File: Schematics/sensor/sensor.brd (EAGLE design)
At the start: 27.6 x 22.9 mm, 9 parts

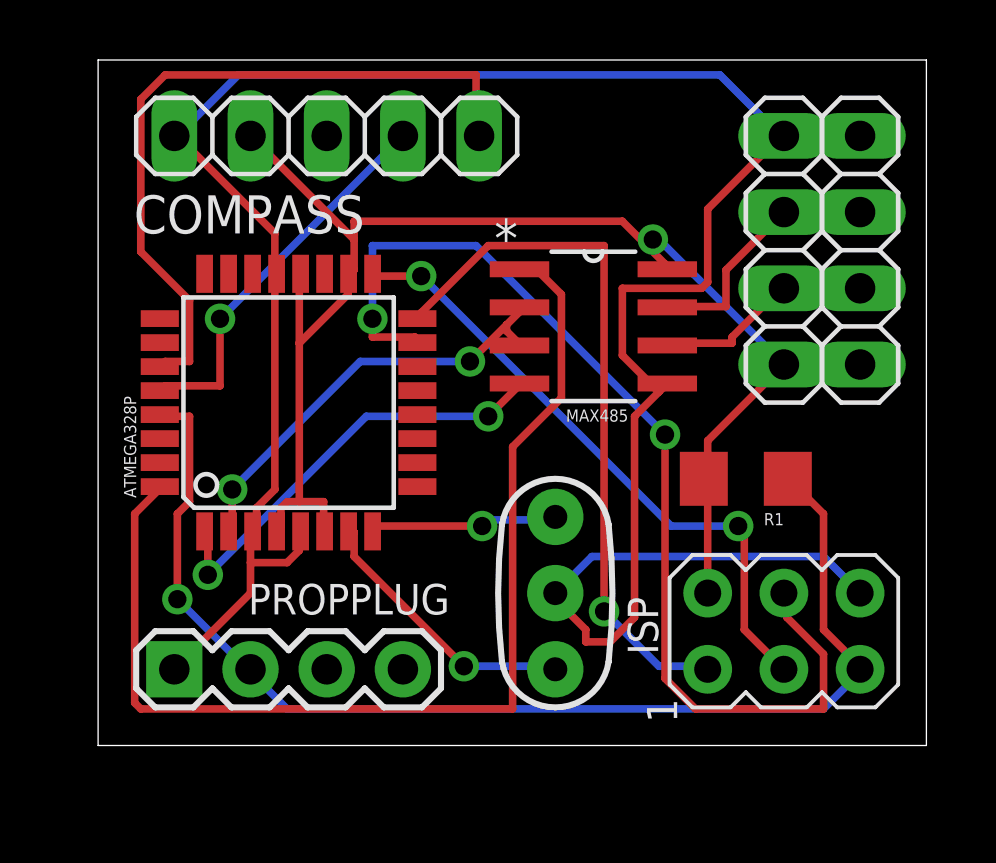
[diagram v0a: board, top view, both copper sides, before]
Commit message: Changed headers for 485 bus and added more labels.
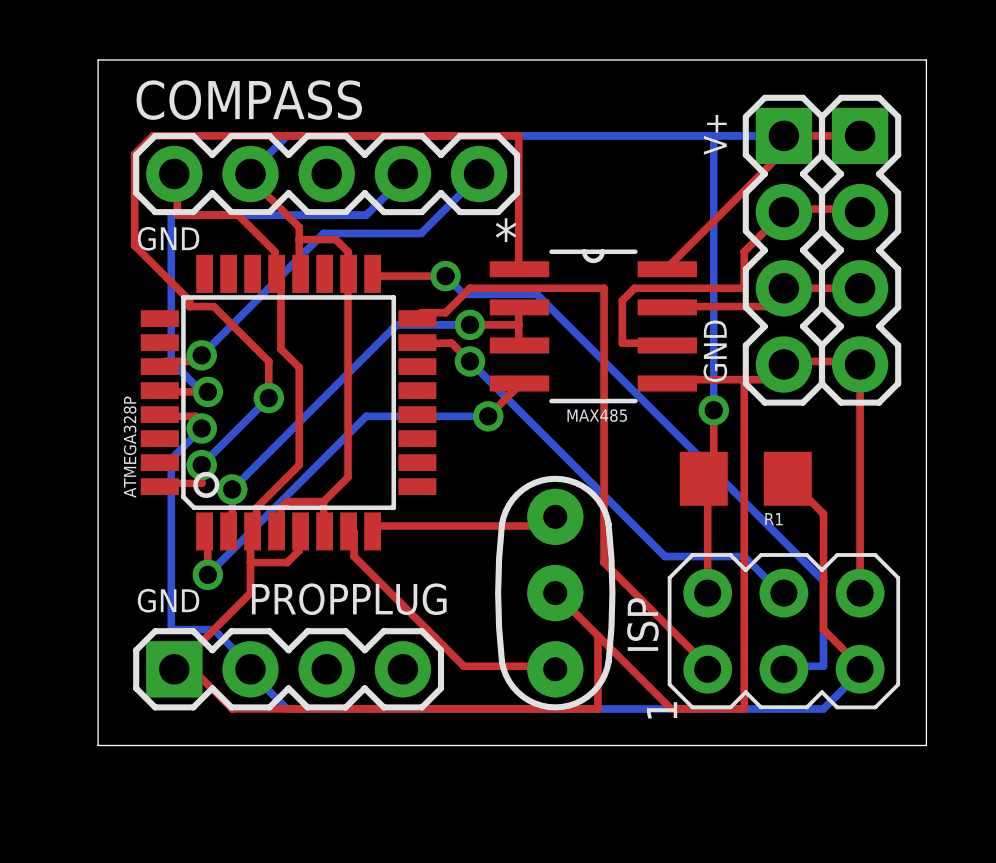
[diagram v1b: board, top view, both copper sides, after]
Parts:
- COMPASS: device pinhead:1X05 -> SparkFun-Connectors:1X05
- JP1, JP2: device pinhead:1X04 -> SparkFun-Connectors:1X04
- moved COMPASS 5.24 mm to (2.54, 19.1)
- moved JP1 4.58 mm to (22.9, 20.3), turned to 270 degrees
- moved JP2 4.58 mm to (25.4, 20.3), turned to 270 degrees
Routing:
- net N$5: track 35.3 -> 15.7 mm, vias 2 -> 1
- net SDA: track 24.1 -> 13.4 mm, vias 0 -> 1
- net 5V: track 49.7 -> 60.3 mm
- net GND: track 84.0 -> 74.3 mm
- net N$7: track 7.32 -> 13.0 mm
- net SCL: track 12.9 -> 16.5 mm
- net RO: track 36.5 -> 33.2 mm, vias 0 -> 2
- net N$4: track 23.8 -> 20.8 mm, vias 1 -> 0
- net N$3: track 21.1 -> 23.5 mm, vias 2 -> 1
- net N$8: track 8.59 -> 7.04 mm
- net RESET: track 39.6 -> 41.0 mm
- net N$2: track 6.34 -> 6.46 mm, vias 1 -> 0
- net N$1: vias 1 -> 0
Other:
- board text added: "GND"
- board text added: "V+"

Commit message: Made sensor PCB smaller. Removed through hole circuit.
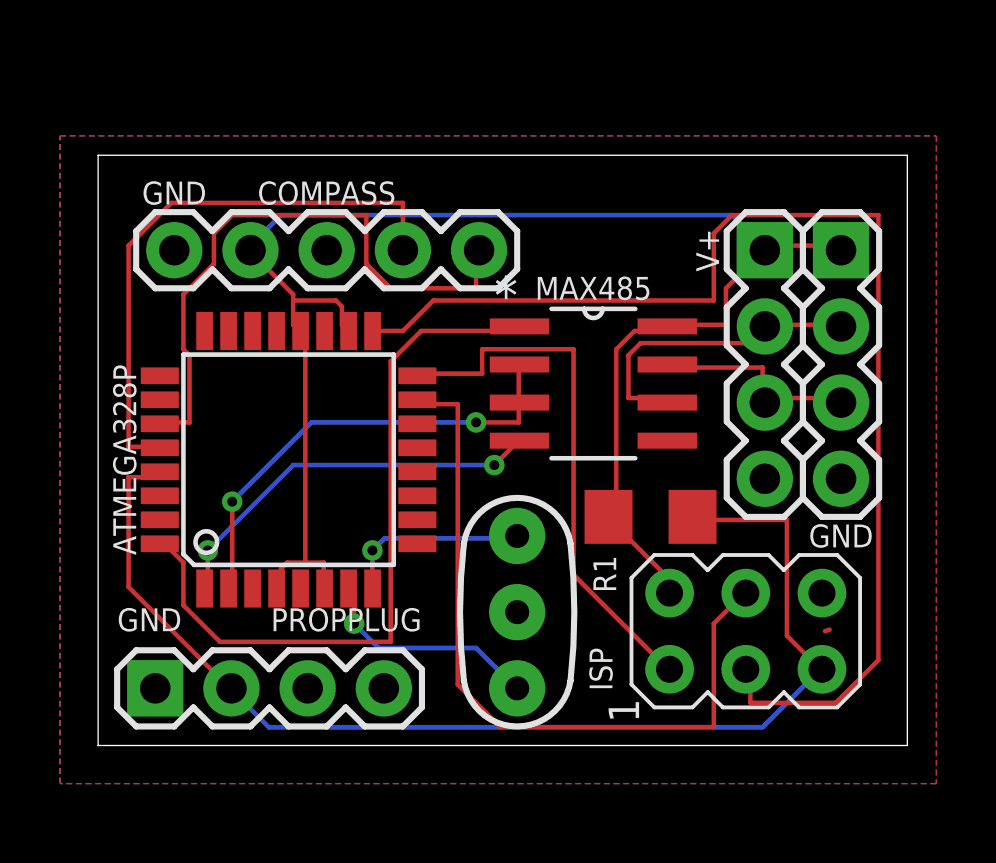
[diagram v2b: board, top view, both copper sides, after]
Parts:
- Y1: value (none) -> 16MHz
- moved JP1 3.86 mm to (22.2, 16.5)
- moved JP2 3.86 mm to (24.8, 16.5)
- moved R1 3.42 mm to (18.4, 7.62)
- moved COMPASS 2.54 mm to (2.54, 16.5)
- moved MAX485 1.91 mm to (16.5, 12.1)
- moved ATMEGA328P 1.90 mm to (6.35, 9.53)
- moved Y1 1.42 mm to (14.0, 4.45)
- moved ISP 1.27 mm to (21.6, 3.81)
- moved PROPPLUG 0.90 mm to (1.91, 1.91)
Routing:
- net GND: track 74.3 -> 0.16 mm
- net N$3: track 23.5 -> 40.7 mm, vias 1 -> 0
- net N$5: track 15.7 -> 24.8 mm, vias 1 -> 0
- net RO: track 33.2 -> 24.1 mm, vias 2 -> 0
- net SDA: track 13.4 -> 20.1 mm, vias 1 -> 0
- net 5V: track 60.3 -> 54.2 mm, vias 1 -> 0
- net N$4: track 20.8 -> 18.0 mm
- net SCL: track 16.5 -> 19.1 mm, vias 1 -> 0
- net N$7: track 13.0 -> 10.6 mm
- net N$1: track 9.32 -> 7.58 mm, vias 0 -> 1
- net RESET: track 41.0 -> 39.4 mm, vias 1 -> 0
- net DI: track 14.6 -> 13.2 mm
- net RW: track 14.5 -> 15.6 mm
- net N$2: track 6.46 -> 6.28 mm, vias 0 -> 1
- added copper zone on layer 1, net GND
- added copper zone on layer 16, net GND
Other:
- board size 27.6 x 22.9 mm -> 27 x 19.7 mm

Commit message: Top/bottom ground planes weren't connected. Added via to connect them.
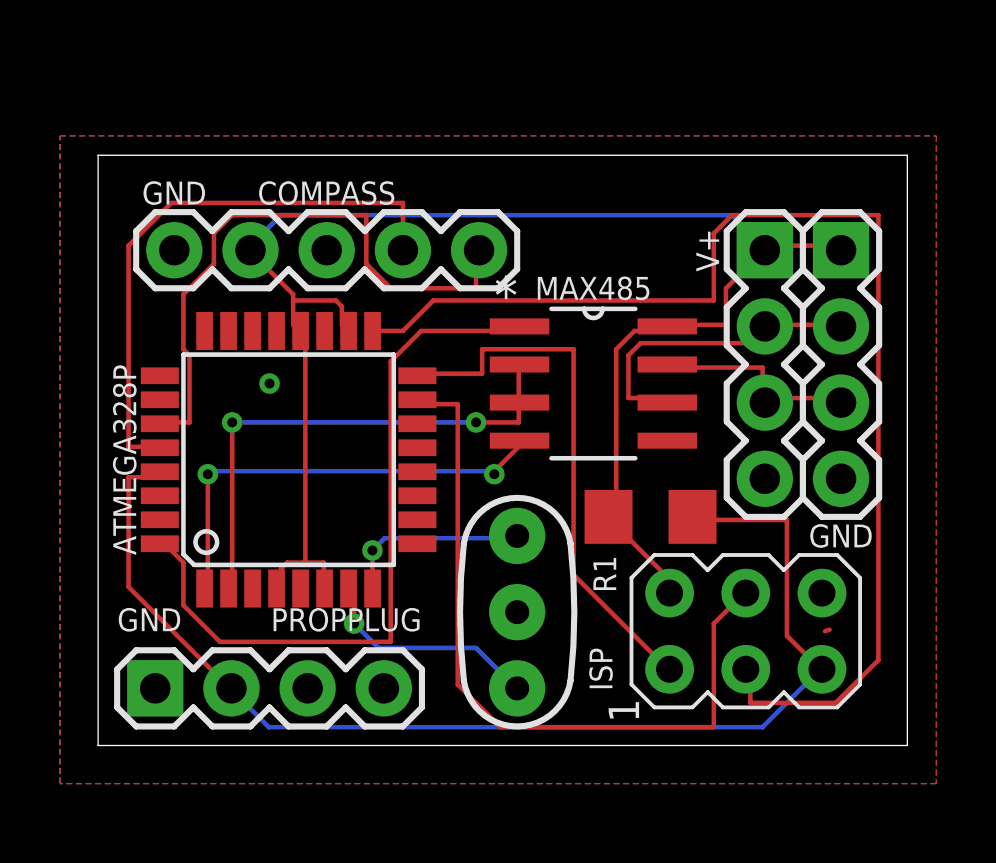
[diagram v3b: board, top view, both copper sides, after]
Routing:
- net DI: track 13.2 -> 15.1 mm
- net RW: track 15.6 -> 17.1 mm
- net GND: track 0.16 -> 0.80 mm, vias 0 -> 1
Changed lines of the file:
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@@
 </polygon>
 <wire x1="24.384" y1="3.8608" x2="24.22995" y2="3.81" width="0.1524" layer="1"/>
-<wire x1="5.95" y1="13.8176" x2="2.54" y2="16.51" width="0" layer="19" extent="1-1"/>
+<wire x1="22.7584" y1="8.9408" x2="22.7584" y2="8.83919375" width="0.1524" layer="1"/>
+<wire x1="22.7584" y1="8.9408" x2="22.225" y2="8.89" width="0.1524" layer="1"/>
+<via x="5.715" y="12.065" extent="1-16" drill="0.3302"/>
 </signal>
 <signal name="5V">
@@
 <contactref element="MAX485" pad="2"/>
 <contactref element="ATMEGA328P" pad="2"/>
-<wire x1="4.4704" y1="8.128" x2="4.4704" y2="5.2832" width="0.1524" layer="1"/>
-<wire x1="7.112" y1="10.7696" x2="4.4704" y2="8.128" width="0.1524" layer="16"/>
-<wire x1="12.5984" y1="10.7696" x2="7.112" y2="10.7696" width="0.1524" layer="16"/>
+<wire x1="4.4704" y1="10.7696" x2="4.4704" y2="5.2832" width="0.1524" layer="1"/>
 <wire x1="14.0208" y1="10.7696" x2="12.5984" y2="10.7696" width="0.1524" layer="1"/>
 <wire x1="14.0208" y1="11.3792" x2="14.0208" y2="10.7696" width="0.1524" layer="1"/>
@@
 <wire x1="14.0208" y1="12.5984" x2="14.0462" y2="12.7" width="0.1524" layer="1"/>
 <wire x1="14.0208" y1="11.5824" x2="14.0462" y2="11.43" width="0.1524" layer="1"/>
-<via x="4.4704" y="8.128" extent="1-16" drill="0.3302"/>
+<via x="4.4704" y="10.7696" extent="1-16" drill="0.3302"/>
 <via x="12.5984" y="10.7696" extent="1-16" drill="0.3302"/>
+<wire x1="4.4704" y1="10.7696" x2="12.5984" y2="10.7696" width="0.1524" layer="16"/>
 </signal>
 <signal name="N$7">
@@
 <contactref element="MAX485" pad="4"/>
 <contactref element="ATMEGA328P" pad="1"/>
-<wire x1="3.6576" y1="6.5024" x2="3.6576" y2="5.2832" width="0.1524" layer="1"/>
-<wire x1="6.5024" y1="9.3472" x2="3.6576" y2="6.5024" width="0.1524" layer="16"/>
-<wire x1="13.208" y1="9.3472" x2="6.5024" y2="9.3472" width="0.1524" layer="16"/>
-<wire x1="14.0208" y1="10.16" x2="13.208" y2="9.3472" width="0.1524" layer="1"/>
+<wire x1="3.6576" y1="9.0424" x2="3.6576" y2="5.2832" width="0.1524" layer="1"/>
 <wire x1="3.6576" y1="5.2832" x2="3.55" y2="5.2324" width="0.1524" layer="1"/>
+<via x="3.6576" y="9.0424" extent="1-16" drill="0.3302"/>
+<via x="13.208" y="9.0424" extent="1-16" drill="0.3302"/>
+<wire x1="14.0208" y1="9.9568" x2="13.208" y2="9.144" width="0.1524" layer="1"/>
+<wire x1="14.0208" y1="10.16" x2="14.0208" y2="9.9568" width="0.1524" layer="1"/>
+<wire x1="13.208" y1="9.144" x2="13.208" y2="9.0424" width="0.1524" layer="1"/>
 <wire x1="14.0208" y1="10.16" x2="14.0462" y2="10.16" width="0.1524" layer="1"/>
-<via x="3.6576" y="6.5024" extent="1-16" drill="0.3302"/>
-<via x="13.208" y="9.3472" extent="1-16" drill="0.3302"/>
+<wire x1="3.6576" y1="9.144" x2="13.208" y2="9.144" width="0.1524" layer="16"/>
+<wire x1="13.208" y1="9.144" x2="13.208" y2="9.0424" width="0.1524" layer="16"/>
+<wire x1="3.6576" y1="9.144" x2="3.6576" y2="9.0424" width="0.1524" layer="16"/>
 </signal>
 <signal name="RO">

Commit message: RX and TX for PROPPLUG weren't connected. they are now.
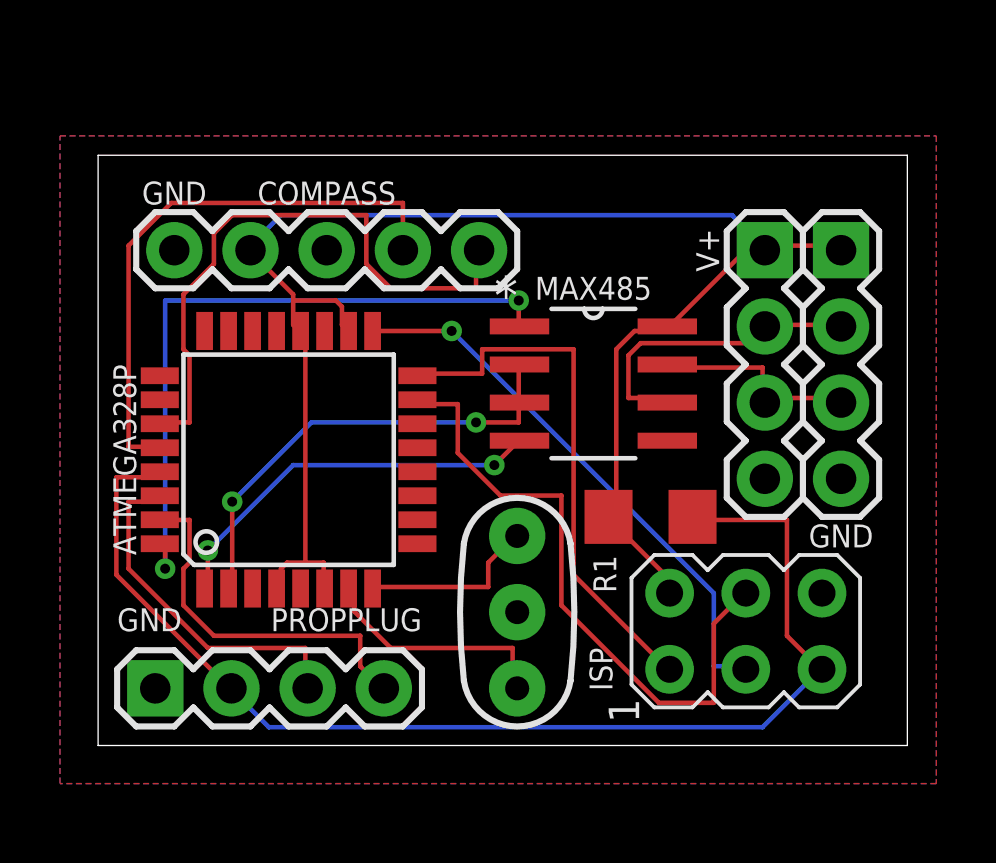
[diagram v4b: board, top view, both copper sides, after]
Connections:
- net N$6: now also ATMEGA328P.30
- net N$9: now also ATMEGA328P.31
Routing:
- net N$3: track 40.7 -> 18.6 mm, vias 0 -> 1
- net N$9: track 0.00 -> 12.3 mm
- net N$6: track 0.00 -> 11.8 mm
- net N$5: track 24.8 -> 21.3 mm
- net DI: track 15.1 -> 13.2 mm
- net RW: track 17.1 -> 15.6 mm
- net RO: track 24.1 -> 22.6 mm, vias 0 -> 2
- net GND: track 0.80 -> 0.00 mm, vias 1 -> 0
- net 5V: track 54.2 -> 53.4 mm
- net RESET: track 39.4 -> 40.0 mm
- net N$1: track 7.58 -> 8.05 mm, vias 1 -> 0
- net N$2: track 6.28 -> 5.99 mm, vias 1 -> 0

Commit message: Revision by Caleb
Changed programming connectors to be on the surface as pads only for
programming with another board.
Rearranged the board to minimize the size as much as possible.
Dimensions are .95 x .65
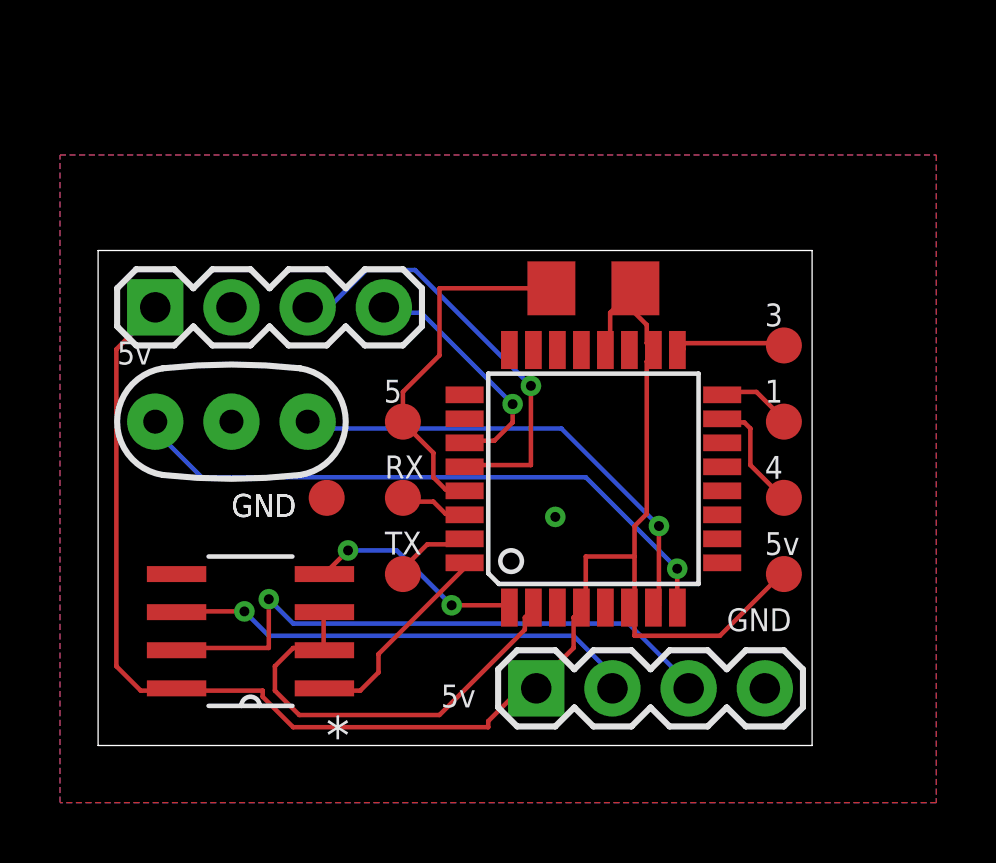
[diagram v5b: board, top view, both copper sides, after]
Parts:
- removed COMPASS: (no value), SparkFun-Connectors:1X05
- removed ISP: AVRISP-6, adafruit:AVRISP
- removed PROPPLUG: (no value), SparkFun-Connectors:1X04
- added 15P, 16P, 17P, 5VP, GP, RST, RX, TX: PTR1TP12R, testpad:TP12R
- moved JP2 22.9 mm to (1.91, 14.6), turned to 0 degrees
- moved JP1 16.5 mm to (14.6, 1.91), turned to 0 degrees
- moved MAX485 14.1 mm to (5.08, 3.81), turned to 180 degrees
- moved Y1 11.4 mm to (4.45, 10.8), turned to 180 degrees
- moved ATMEGA328P 10.2 mm to (16.5, 8.89)
- moved R1 7.85 mm to (16.5, 15.2), turned to 0 degrees
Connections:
- net 5V: now also 5VP.TP; no longer COMPASS.2, ISP.2
- net GND: now also GP.TP, JP2.2; no longer COMPASS.1, ISP.6, JP2.4, PROPPLUG.1
- net N$3: now also 17P.TP; no longer ISP.3
- net N$4: now also 16P.TP; no longer ISP.1
- net N$5: now also 15P.TP; no longer ISP.4
- net N$6: now also RX.TP; no longer PROPPLUG.3
- net N$7: no longer JP2.2
- net N$8: no longer JP2.3
- net N$9: now also TX.TP; no longer PROPPLUG.4
- net RESET: now also RST.TP; no longer ISP.5, PROPPLUG.2
- net SCL: now also JP2.3; no longer COMPASS.4
- net SDA: now also JP2.4; no longer COMPASS.5
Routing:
- net RESET: track 40.0 -> 12.2 mm
- net N$5: track 21.3 -> 3.86 mm
- net RO: track 22.6 -> 6.90 mm, vias 2 -> 0
- net N$4: track 18.0 -> 2.53 mm
- net N$2: track 5.99 -> 21.0 mm, vias 0 -> 1
- net N$3: track 18.6 -> 3.78 mm, vias 1 -> 0
- net N$8: track 7.06 -> 20.1 mm, vias 0 -> 1
- net SDA: track 20.1 -> 8.18 mm, vias 0 -> 1
- net N$9: track 12.3 -> 2.73 mm
- net N$6: track 11.8 -> 2.37 mm
- net N$1: track 8.05 -> 16.0 mm, vias 0 -> 1
- net DI: track 13.2 -> 7.28 mm
- net N$7: track 10.6 -> 15.9 mm, vias 0 -> 1
- net SCL: track 19.1 -> 14.4 mm, vias 0 -> 1
- net 5V: track 53.4 -> 55.9 mm
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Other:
- board size 27 x 19.7 mm -> 23.8 x 16.5 mm
- board text added: "1"
- board text added: "3"
- board text added: "4"
- board text added: "5"
- board text added: "5v"
- board text removed: "V+"

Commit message: PCB updates
changed sensor PCB to 3.0
changed Node PCB to 2.0 and parts list to go with it (Sach, can you
look over the schematic, board, and parts list that I have so far to
make sure I have everything correct?)
added Base Station PCB 0.5
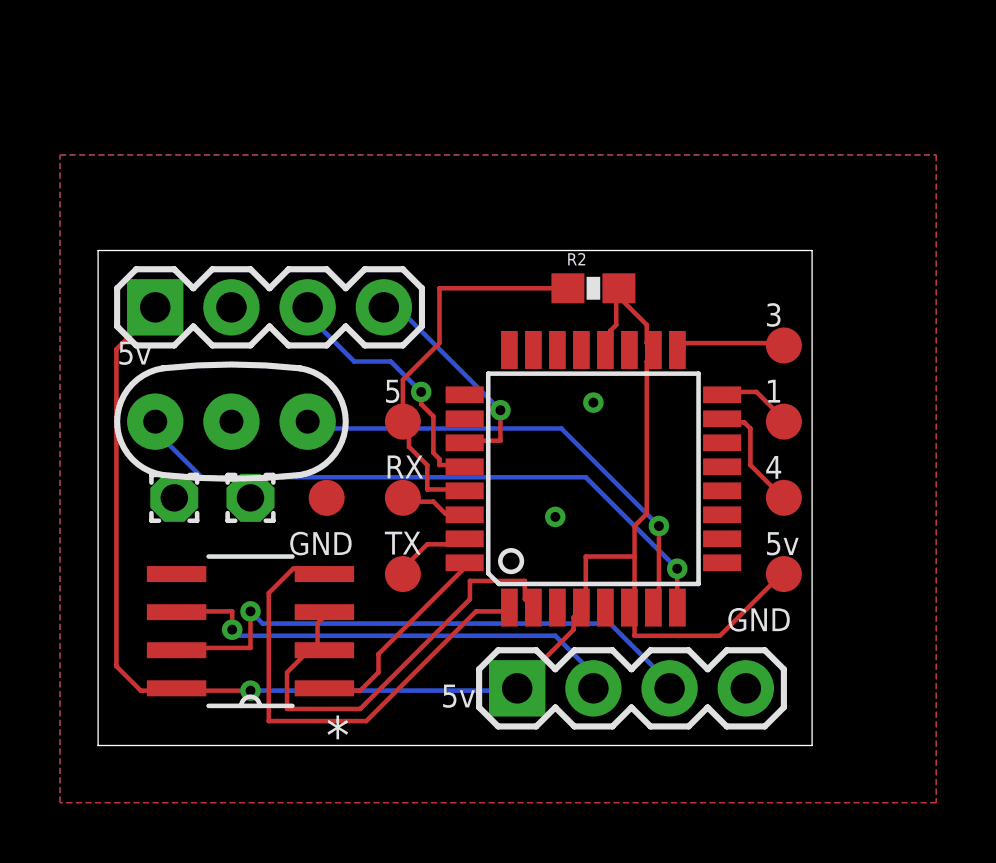
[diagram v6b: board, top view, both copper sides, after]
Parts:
- removed R1: 10K, SparkFun-Passives:1206
- added PAD1, PAD2: (no value), wirepad:1,6/0,9
- added R2: 10K, SparkFun-Passives:0603-RES
- moved JP1 0.63 mm to (14.0, 1.91)
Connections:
- net 5V: now also R2.2; no longer R1.2
- net RESET: now also R2.1; no longer R1.1
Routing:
- net DI: track 7.28 -> 16.2 mm, vias 2 -> 0
- net SCL: track 14.4 -> 8.71 mm
- net 5V: track 55.9 -> 54.0 mm, vias 0 -> 1
- net N$8: track 20.1 -> 18.9 mm
- net RW: track 14.7 -> 15.6 mm
- net RESET: track 12.2 -> 13.1 mm
- net SDA: track 8.18 -> 7.61 mm
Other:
- board text added: "SPSen 3.0"
